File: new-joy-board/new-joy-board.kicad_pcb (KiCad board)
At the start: 2 copper layers, 3 parts, among them J1 Screw_Terminal_01x02, U1 AZReady_ESP32, U2 dc_dc_converter

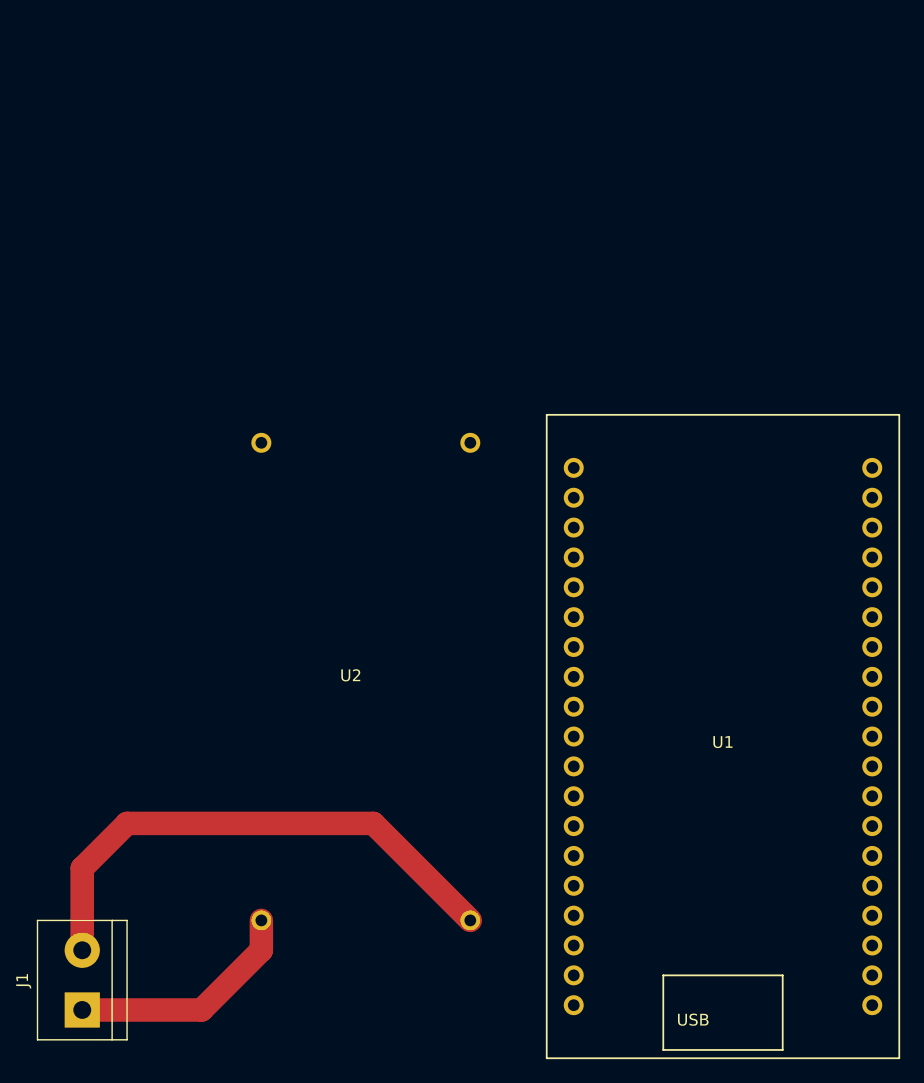
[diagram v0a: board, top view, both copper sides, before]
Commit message: 3V3 power regulator and i2c0 bus
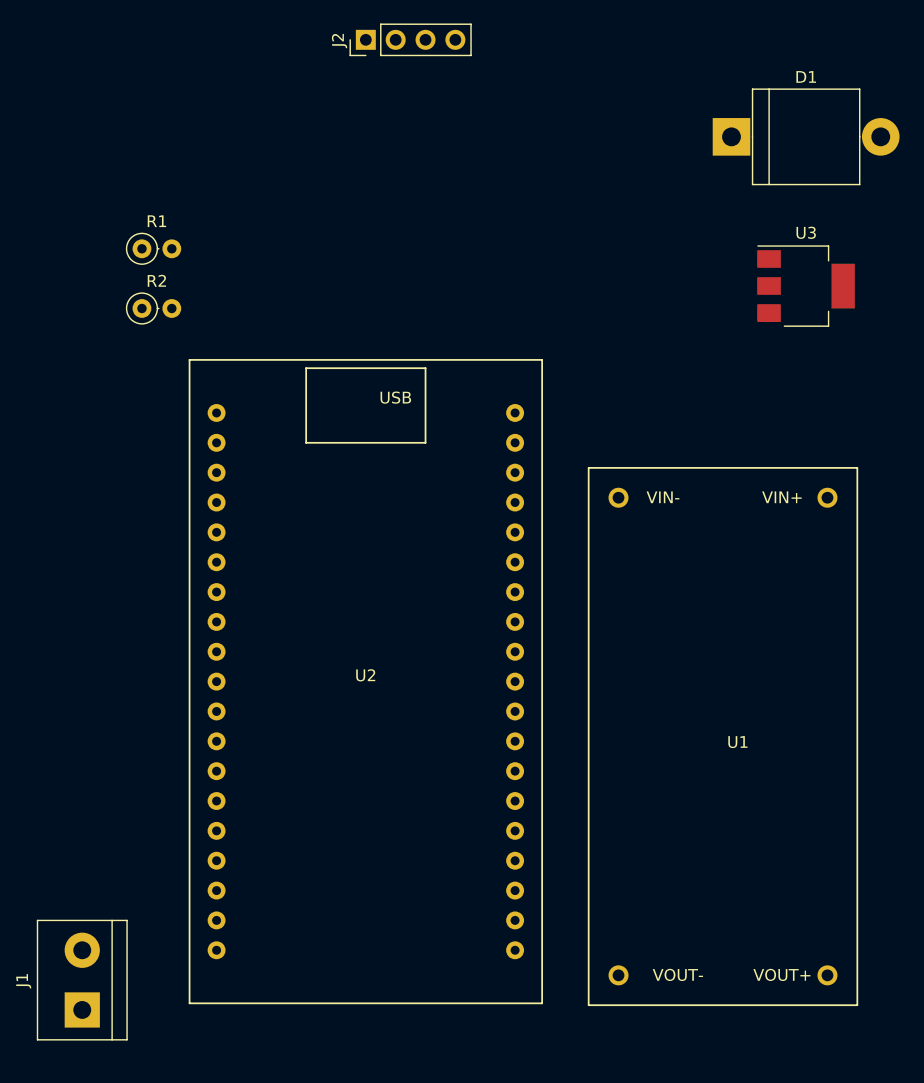
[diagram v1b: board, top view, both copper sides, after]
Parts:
- added D1: D, Diodes_THT:D_5KPW_P12.70mm_Horizontal, F.Cu at (149.2, 54.0)
- added J2: I2C_CONN, Pin_Headers:Pin_Header_Straight_1x04_Pitch2.54mm, F.Cu at (118.1, 45.7)
- added R1: R, Resistors_THT:R_Axial_DIN0207_L6.3mm_D2.5mm_P2.54mm_Vertical, F.Cu at (99.1, 63.5)
- added R2: R, Resistors_THT:R_Axial_DIN0207_L6.3mm_D2.5mm_P2.54mm_Vertical, F.Cu at (99.1, 68.6)
- added U3: AZ1117-3.3, TO_SOT_Packages_SMD:SOT-223, F.Cu at (155.6, 66.7)
- U1: value AZReady_ESP32 -> dc_dc_converter; footprint new-joy:AZReady_ESP32 -> new-joy:dc_dc_converter
- U2: value dc_dc_converter -> AZReady_ESP32; footprint new-joy:dc_dc_converter -> new-joy:AZReady_ESP32
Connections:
- U1 pad 1: Net-(U1-Pad1) -> +12V
- U1 pad 2: Net-(U1-Pad2) -> GNDPWR
- U1 pad 3: Net-(U1-Pad3) -> +5V
- U1 pad 4: Net-(U1-Pad4) -> GND
- U2 pad 1: +12V -> Net-(U2-Pad1)
- U2 pad 2: GNDPWR -> Net-(U2-Pad2)
- U2 pad 3: +5V -> Net-(U2-Pad3)
- U2 pad 4: GND -> Net-(U2-Pad4)
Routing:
- net GNDPWR: track 45.0 -> 0.00 mm
- net +12V: track 19.9 -> 0.00 mm

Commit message: Worked on design, including DMX and buffered I2C
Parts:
- added C1: 10uF, Capacitors_SMD:CP_Elec_5x5.3, F.Cu at (88.9, 72.4)
- added C2: 100nF, Capacitors_SMD:C_1210_HandSoldering, B.Cu at (65.4, 61.0)
- added J3: I2C_CONN_1, Pin_Headers:Pin_Header_Straight_1x04_Pitch2.54mm, F.Cu at (80.0, 155.6)
- added J4: I2C_CONN_2, Pin_Headers:Pin_Header_Straight_1x04_Pitch2.54mm, F.Cu at (80.0, 165.1)
- added J5: I2C_CONN_3, Pin_Headers:Pin_Header_Straight_1x04_Pitch2.54mm, F.Cu at (80.0, 175.9)
- added J6: DMX, Connectors_Terminal_Blocks:TerminalBlock_bornier-3_P5.08mm, F.Cu at (23.5, 170.2)
- added R3: 133, Resistors_SMD:R_1210_HandSoldering, F.Cu at (31.1, 159.4)
- added RV1: 10K, Potentiometers:Potentiometer_Trimmer_Piher_PT-15v12.5_Horizontal_Px12.5mm_Py10.0mm, F.Cu at (55.9, 145.4)
- added RV2: 10K, Potentiometers:Potentiometer_Trimmer_Piher_PT-15v12.5_Horizontal_Px12.5mm_Py10.0mm, F.Cu at (55.9, 165.1)
- added U4: P82B715, new-joy:P82B715D, F.Cu at (76.2, 136.5)
- added U5: MPU6050_Breakout, new-joy:MPU6050_Breakout, F.Cu at (47.0, 128.3)
- added U6: MAX3072E, Housings_SOIC:SOIC-8_3.9x4.9mm_Pitch1.27mm, F.Cu at (31.1, 150.5)
- J1: value Screw_Terminal_01x02 -> BAT
- J2: value I2C_CONN -> I2C_CONN_4
- R1, R2: value R -> 4K7; footprint Resistors_THT:R_Axial_DIN0207_L6.3mm_D2.5mm_P2.54mm_Vertical -> Resistors_SMD:R_1210_HandSoldering
- U3: moved to B.Cu
- moved J2 106.7 mm to (80.0, 145.4), turned to 270 degrees
- moved U1 99.4 mm to (60.3, 59.1), turned to 90 degrees
- moved J1 96.9 mm to (28.6, 56.8), turned to 270 degrees
- moved U3 79.8 mm to (76.2, 58.4)
- moved R1 75.1 mm to (43.8, 114.3)
- moved U2 67.4 mm to (51.4, 90.2), turned to 270 degrees
- moved R2 67.1 mm to (45.7, 109.2)
- moved D1 60.3 mm to (88.9, 53.3), turned to 270 degrees
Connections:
- J1 pad 2: GNDPWR -> GND
- J2 pad 1: /SDA0 -> /SDA0BUF
- J2 pad 2: +3V3 -> +5V
- J2 pad 3: /SCL0 -> /SCL0BUF
- R1 pad 2: /SCL0 -> /SCL0ESP
- R2 pad 2: /SDA0 -> /SDA0ESP
- U1 pad 2: GNDPWR -> GND
- U2 pad 12: /SDA0 -> /SDA0ESP
- U2 pad 13: /SCL0 -> /SCL0ESP
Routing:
- net +5V: track 0.00 -> 366.8 mm, vias 0 -> 3
- net GND: track 0.00 -> 265.6 mm, vias 0 -> 3
- net +3V3: track 0.00 -> 209.4 mm, vias 0 -> 3
- net /SDA0BUF: track 0.00 -> 81.0 mm
- net /SCL0BUF: track 0.00 -> 80.3 mm
- net /SCL0ESP: track 0.00 -> 80.3 mm
- net /SDA0ESP: track 0.00 -> 59.8 mm
- net Net-(J6-Pad3): track 0.00 -> 17.8 mm
- net Net-(J6-Pad2): track 0.00 -> 17.8 mm
- net +12V: track 0.00 -> 14.2 mm
- added copper zone on B.Cu, net GND
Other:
- net class pwr: via_dia 2 -> 1
- net class pwr3 added: clearance 0.2, trace_width 0.5, via_dia 0.6, via_drill 0.4
- net class pwr5 added: clearance 0.2, trace_width 0.5, via_dia 0.6, via_drill 0.4

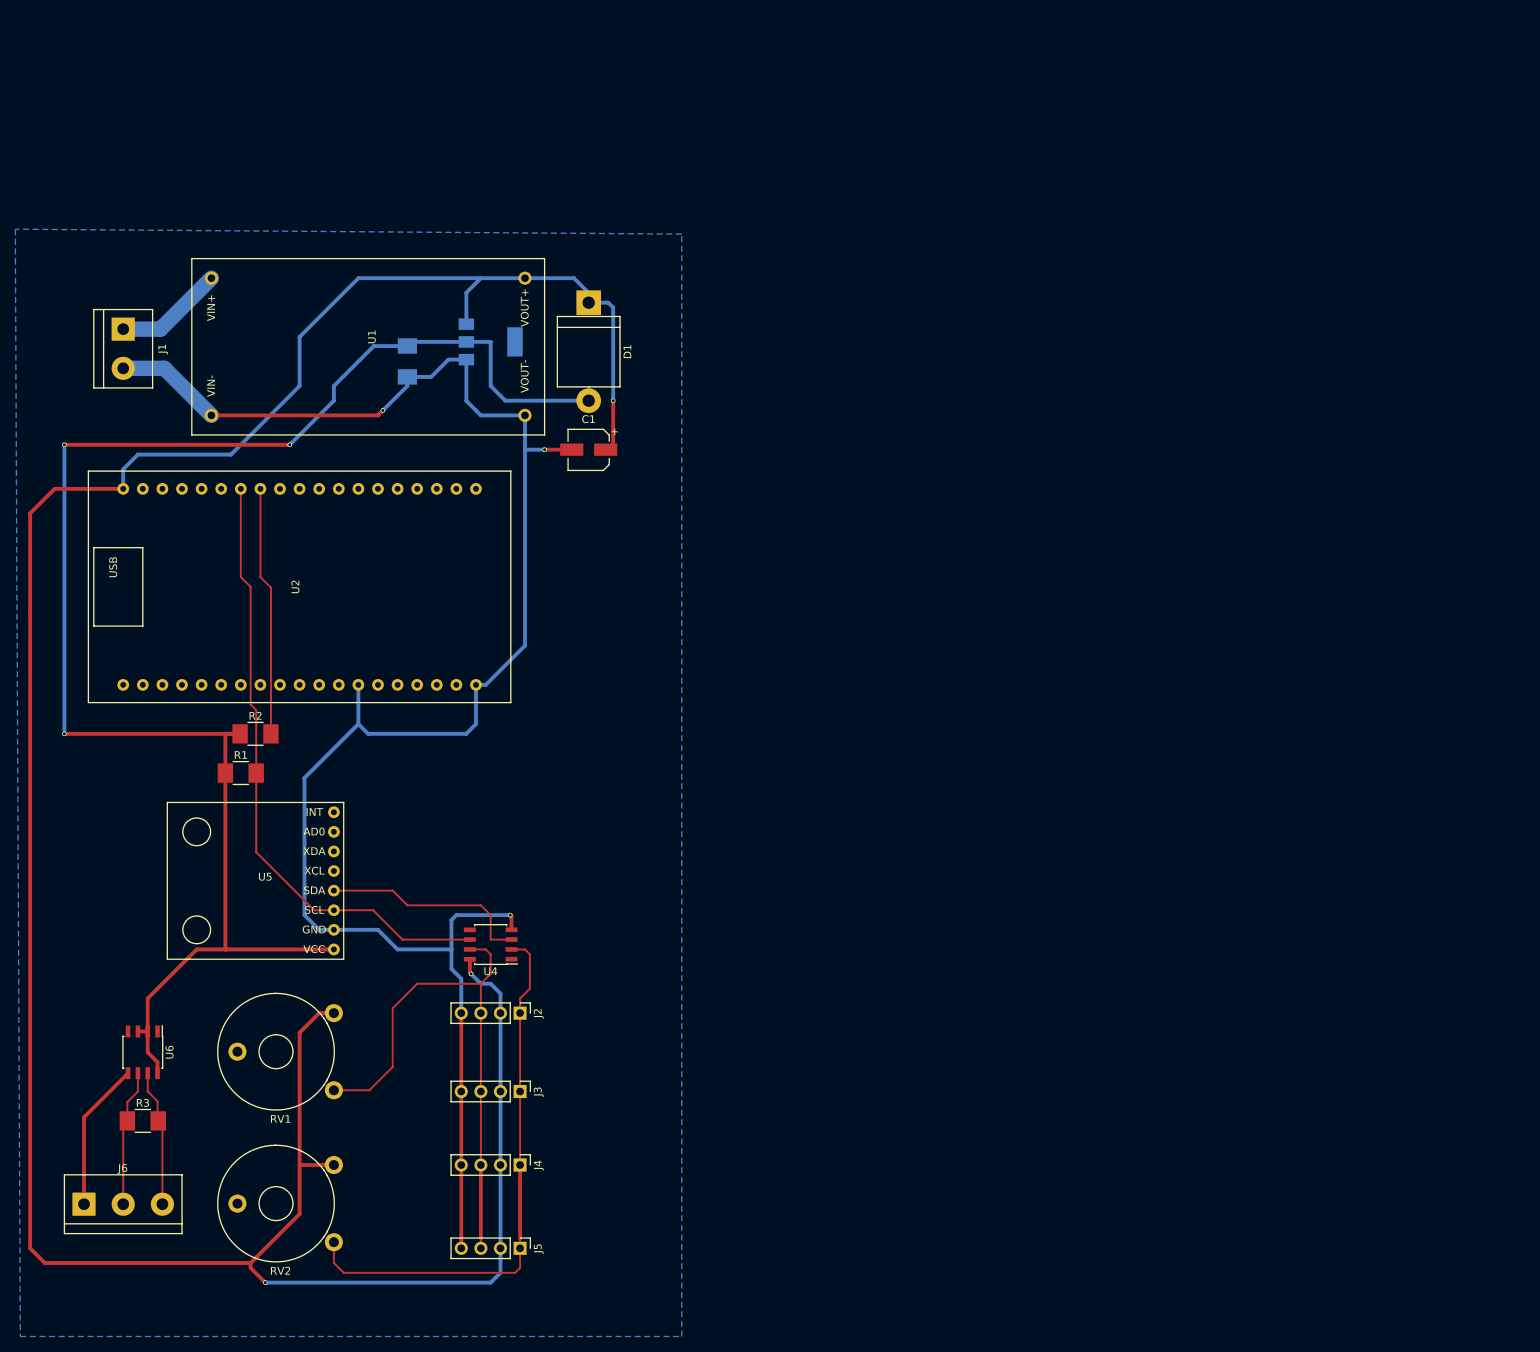
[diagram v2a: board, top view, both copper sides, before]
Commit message: Work on schematic and PCB to mock up real PCB
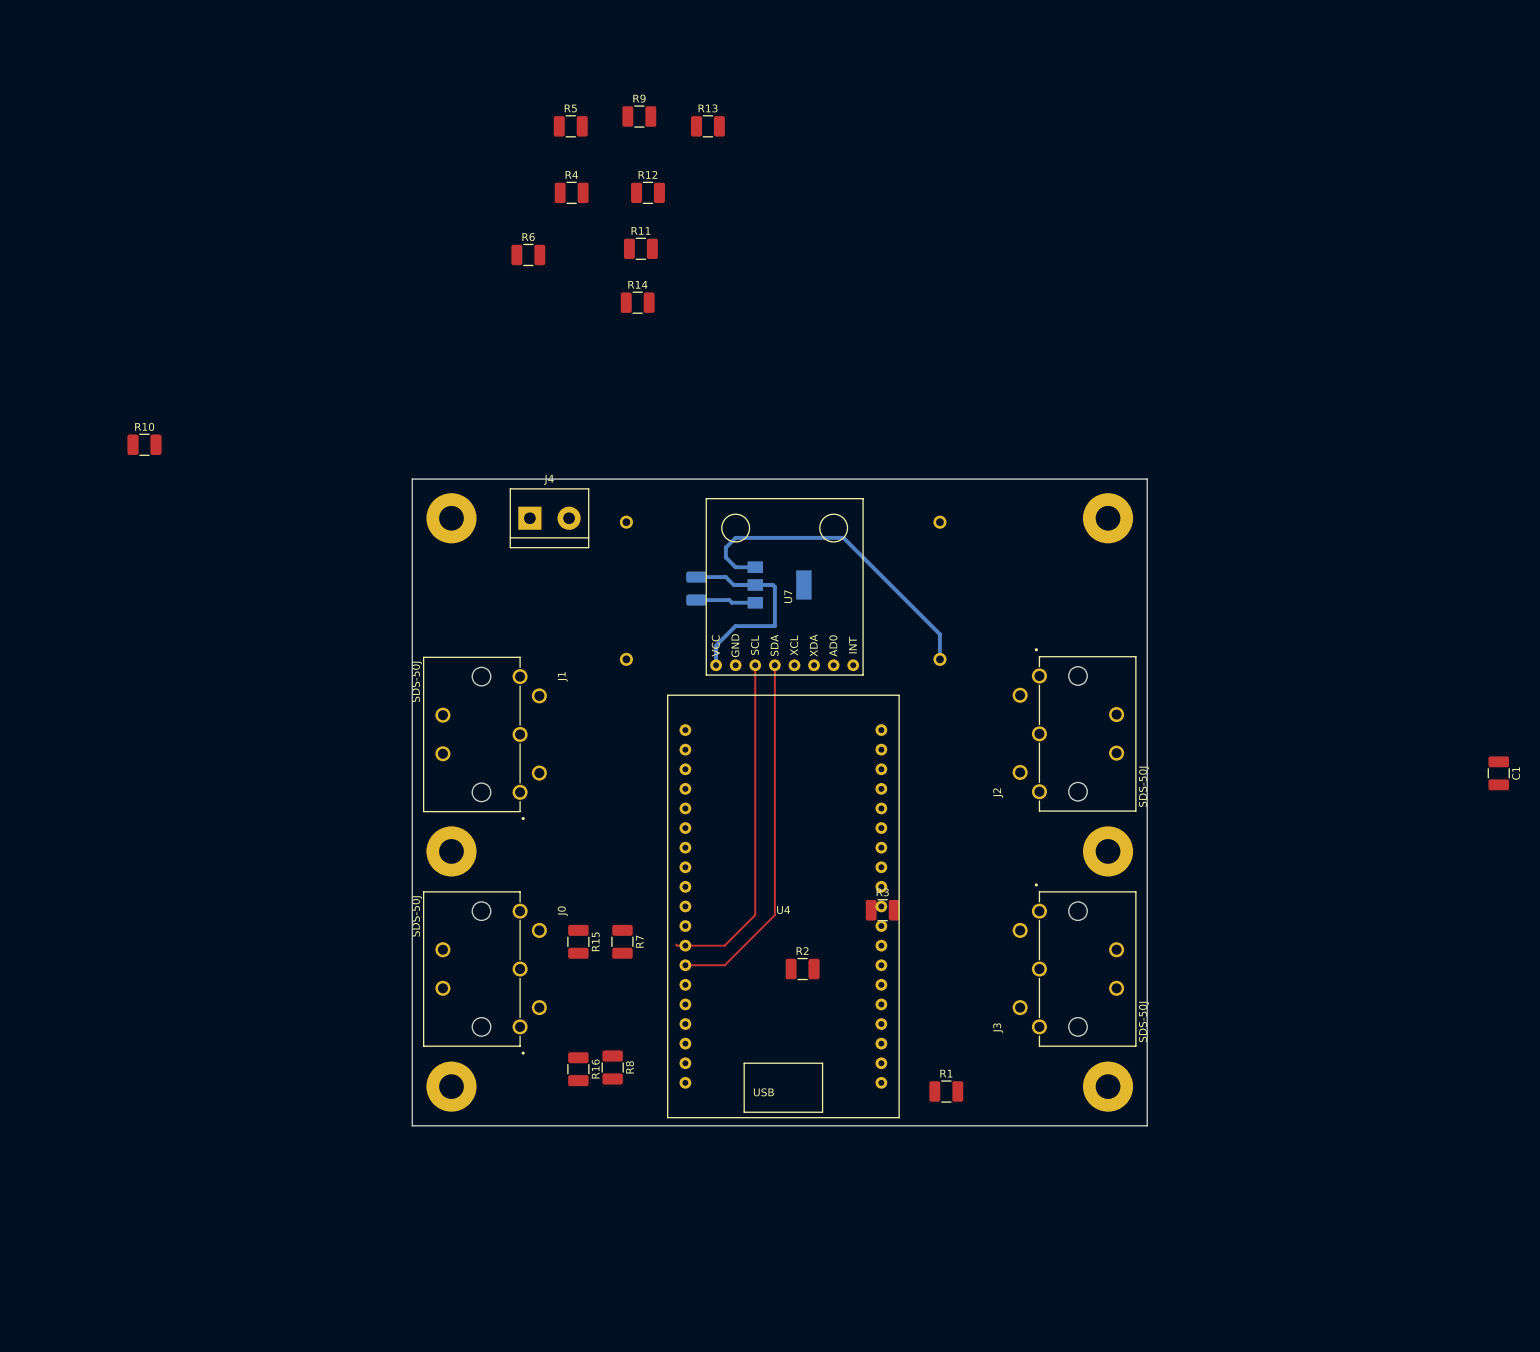
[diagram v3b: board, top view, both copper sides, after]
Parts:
- removed D1: D, Diodes_THT:D_5KPW_P12.70mm_Horizontal
- removed J5: I2C_CONN_3, Pin_Headers:Pin_Header_Straight_1x04_Pitch2.54mm
- removed J6: DMX, Connectors_Terminal_Blocks:TerminalBlock_bornier-3_P5.08mm
- removed RV1, RV2: 10K, Potentiometers:Potentiometer_Trimmer_Piher_PT-15v12.5_Horizontal_Px12.5mm_Py10.0mm
- removed U1: dc_dc_converter, new-joy:dc_dc_converter
- removed U2: AZReady_ESP32, new-joy:AZReady_ESP32
- removed U3: AZ1117-3.3, TO_SOT_Packages_SMD:SOT-223
- added J0: SDS-50J, new-joy:CUI_SDS-50J, F.Cu at (80.0, 139.7)
- added R10: 4K7, Resistor_SMD:R_1210_3225Metric_Pad1.42x2.65mm_HandSolder, F.Cu at (31.3, 71.8)
- added R11: 4K7, Resistor_SMD:R_1210_3225Metric_Pad1.42x2.65mm_HandSolder, F.Cu at (95.7, 46.4)
- added R12: 4K7, Resistor_SMD:R_1210_3225Metric_Pad1.42x2.65mm_HandSolder, F.Cu at (96.6, 39.1)
- added R13: 4K7, Resistor_SMD:R_1210_3225Metric_Pad1.42x2.65mm_HandSolder, F.Cu at (104.4, 30.5)
- added R14: 4K7, Resistor_SMD:R_1210_3225Metric_Pad1.42x2.65mm_HandSolder, F.Cu at (95.2, 53.3)
- added R15: 4K7, Resistor_SMD:R_1210_3225Metric_Pad1.42x2.65mm_HandSolder, F.Cu at (87.6, 136.2)
- added R16: 4K7, Resistor_SMD:R_1210_3225Metric_Pad1.42x2.65mm_HandSolder, F.Cu at (87.6, 152.7)
- added R4: 4K7, Resistor_SMD:R_1210_3225Metric_Pad1.42x2.65mm_HandSolder, F.Cu at (86.7, 39.1)
- added R5: 4K7, Resistor_SMD:R_1210_3225Metric_Pad1.42x2.65mm_HandSolder, F.Cu at (86.6, 30.5)
- added R6: 4K7, Resistor_SMD:R_1210_3225Metric_Pad1.42x2.65mm_HandSolder, F.Cu at (81.1, 47.2)
- added R7: 4K7, Resistor_SMD:R_1210_3225Metric_Pad1.42x2.65mm_HandSolder, F.Cu at (93.3, 136.2)
- added R8: 4K7, Resistor_SMD:R_1210_3225Metric_Pad1.42x2.65mm_HandSolder, F.Cu at (92.0, 152.5)
- added R9: 4K7, Resistor_SMD:R_1210_3225Metric_Pad1.42x2.65mm_HandSolder, F.Cu at (95.5, 29.2)
- added REF**: VAL**, new-joy:z_MountPTH_3mm, F.Cu at (71.1, 154.9)
- added REF**: VAL**, new-joy:z_MountPTH_3mm, F.Cu at (71.1, 124.5)
- added REF**: VAL**, new-joy:z_MountPTH_3mm, F.Cu at (71.1, 81.3)
- added REF**: VAL**, new-joy:z_MountPTH_3mm, F.Cu at (156.2, 81.3)
- added REF**: VAL**, new-joy:z_MountPTH_3mm, F.Cu at (156.2, 124.5)
- added REF**: VAL**, new-joy:z_MountPTH_3mm, F.Cu at (156.2, 154.9)
- added U7: MPU6050_Breakout, new-joy:MPU6050_Breakout, F.Cu at (114.3, 91.4)
- C1: footprint Capacitors_SMD:CP_Elec_5x5.3 -> Capacitor_SMD:C_1210_3225Metric_Pad1.42x2.65mm_HandSolder
- C2: footprint Capacitors_SMD:C_1210_HandSoldering -> Capacitor_SMD:C_1210_3225Metric_Pad1.42x2.65mm_HandSolder
- J1: value BAT -> SDS-50J; footprint Connectors_Terminal_Blocks:TerminalBlock_bornier-2_P5.08mm -> new-joy:CUI_SDS-50J
- J2: value I2C_CONN_4 -> SDS-50J; footprint Pin_Headers:Pin_Header_Straight_1x04_Pitch2.54mm -> new-joy:CUI_SDS-50J
- J3: value I2C_CONN_1 -> SDS-50J; footprint Pin_Headers:Pin_Header_Straight_1x04_Pitch2.54mm -> new-joy:CUI_SDS-50J
- J4: value I2C_CONN_2 -> BAT; footprint Pin_Headers:Pin_Header_Straight_1x04_Pitch2.54mm -> TerminalBlock:TerminalBlock_bornier-2_P5.08mm
- R1, R2: footprint Resistors_SMD:R_1210_HandSoldering -> Resistor_SMD:R_1210_3225Metric_Pad1.42x2.65mm_HandSolder
- R3: value 133 -> 4K7; footprint Resistors_SMD:R_1210_HandSoldering -> Resistor_SMD:R_1210_3225Metric_Pad1.42x2.65mm_HandSolder
- U4: value P82B715 -> AZReady_ESP32; footprint new-joy:P82B715D -> new-joy:AZReady_ESP32
- U5: value MPU6050_Breakout -> dc_dc_converter; footprint new-joy:MPU6050_Breakout -> new-joy:dc_dc_converter; moved to B.Cu
- U6: value MAX3072E -> AZ1117-3.3; footprint Housings_SOIC:SOIC-8_3.9x4.9mm_Pitch1.27mm -> Package_TO_SOT_SMD:SOT-223; moved to B.Cu
- moved C1 125.2 mm to (206.8, 114.3), turned to 270 degrees
- moved U6 102.4 mm to (113.6, 89.9), turned to 0 degrees
- moved R1 100.3 mm to (135.3, 155.6)
- moved R3 99.7 mm to (127.0, 132.1)
- moved J4 83.8 mm to (81.3, 81.3), turned to 0 degrees
- moved R2 77.2 mm to (116.6, 139.7)
- moved U5 76.9 mm to (114.1, 90.7), turned to 270 degrees
- moved J2 76.4 mm to (147.3, 109.2), turned to 90 degrees
- moved J1 73.5 mm to (80.0, 109.3)
- moved J3 69.2 mm to (147.3, 139.7), turned to 90 degrees
- moved C2 47.6 mm to (102.9, 90.4)
- moved U4 38.3 mm to (114.1, 131.6), turned to 0 degrees
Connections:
- J1 pad 1: +12V -> GND
- J1 pad 2: GND -> Net-(J1-Pad2)
- J2 pad 1: /SDA0BUF -> GND
- J2 pad 2: +5V -> Net-(J2-Pad2)
- J2 pad 3: /SCL0BUF -> /SCL2BUF
- J2 pad 4: GND -> /SDA2BUF
- J3 pad 1: /SDA0BUF -> GND
- J3 pad 2: +5V -> Net-(J3-Pad2)
- J3 pad 3: /SCL0BUF -> /SCL3BUF
- J3 pad 4: GND -> /SDA3BUF
- J4 pad 1: /SDA0BUF -> +BATT
- J4 pad 2: +5V -> +BATT
- R1 pad 2: /SCL0ESP -> /SCL3ESP
- R2 pad 2: /SDA0ESP -> /SDA3ESP
- R3 pad 1: Net-(J6-Pad2) -> +3V3
- R3 pad 2: Net-(J6-Pad3) -> /SCL2ESP
- U4 pad 2: /SDA0BUF -> Net-(U4-Pad2)
- U4 pad 3: /SDA0ESP -> Net-(U4-Pad3)
- U4 pad 4: GND -> Net-(U4-Pad4)
- U4 pad 6: /SCL0ESP -> Net-(U4-Pad6)
- U4 pad 7: /SCL0BUF -> Net-(U4-Pad7)
- U4 pad 8: +5V -> Net-(U4-Pad8)
- U5 pad 1: +3V3 -> +BATT
- U5 pad 2: GND -> +BATT
- U5 pad 3: /SCL0ESP -> +5V
- U5 pad 4: /SDA0ESP -> GND
- U6 pad 1: Net-(U6-Pad1) -> GND
- U6 pad 3: +3V3 -> +5V
- U6 pad 4: Net-(U2-Pad35) -> (no net)
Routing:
- net +5V: track 366.8 -> 42.3 mm, vias 3 -> 0
- net GND: track 265.6 -> 7.77 mm, vias 3 -> 0
- net +3V3: track 209.4 -> 27.0 mm, vias 3 -> 0
- net /SDA0BUF: track 81.0 -> 0.00 mm
- net /SCL0BUF: track 80.3 -> 0.00 mm
- net /SCL0ESP: track 80.3 -> 44.4 mm
- net Net-(J6-Pad3): track 17.8 -> 0.00 mm
- net Net-(J6-Pad2): track 17.8 -> 0.00 mm
- net +12V: track 14.2 -> 0.00 mm
- net /SDA0ESP: track 59.8 -> 46.7 mm
- removed copper zone on B.Cu, net GND
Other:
- board outline added: 95.2 x 83.8 mm
